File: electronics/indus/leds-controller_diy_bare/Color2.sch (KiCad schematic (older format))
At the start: 19 parts, among them Q2 Q_NPN_BCE, U1 TPS92513

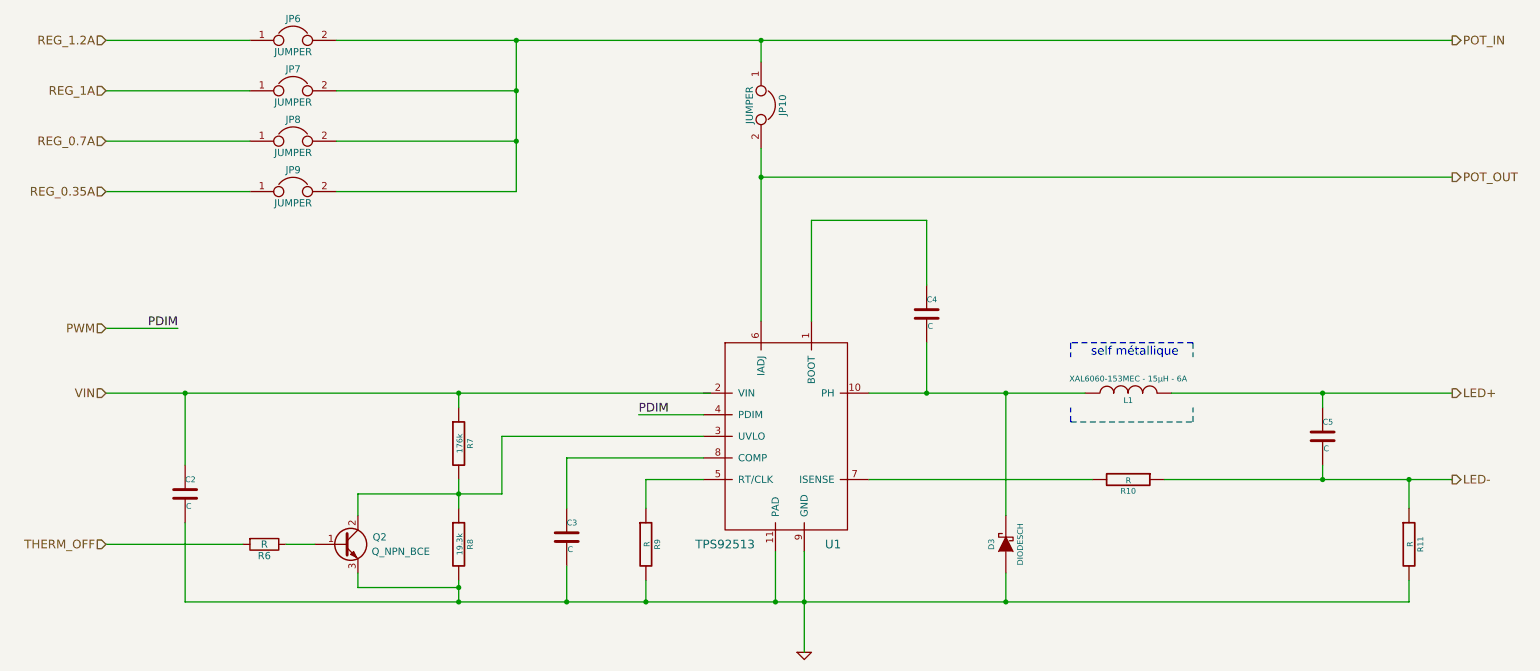
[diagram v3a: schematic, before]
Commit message: Added missing Capa & Resistor values
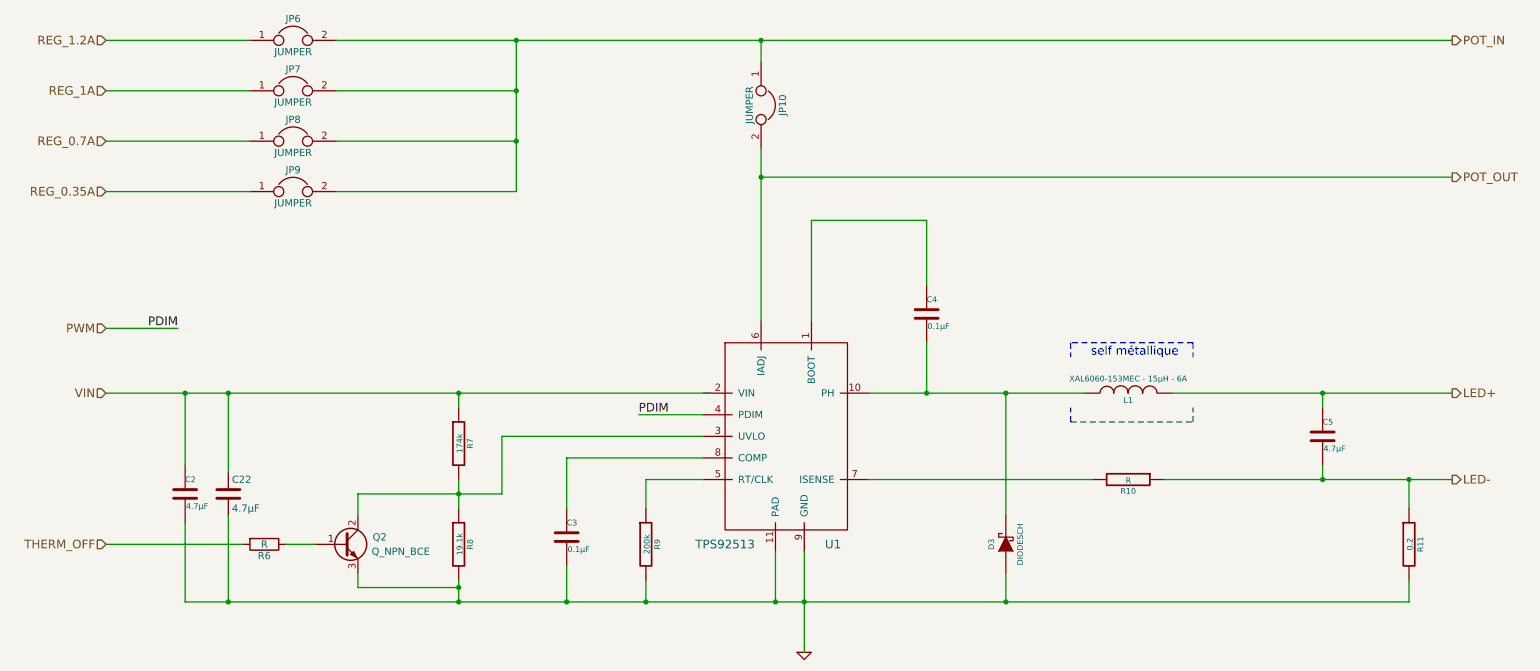
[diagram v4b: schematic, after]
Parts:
- added C22: 4.7µF, symbol C
- C2, C5: value C -> 4.7µF
- C3, C4: value C -> 0.1µF
- R11: value R -> 0.2
- R7: value 176k -> 174k
- R8: value 19.3k -> 19.1k
- R9: value R -> 200k
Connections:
- net GND: now also C22.2
- net VIN: now also C22.1
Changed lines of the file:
@@
 P 1750 4650
 F 0 "C2" H 1750 4750 40  0000 L CNN
-F 1 "C" H 1756 4565 40  0000 L CNN
+F 1 "4.7µF" H 1756 4565 40  0000 L CNN
 F 2 "" H 1788 4500 30  0000 C CNN
 F 3 "" H 1750 4650 60  0000 C CNN
@@
 P 3650 4300
 F 0 "R7" V 3730 4300 40  0000 C CNN
-F 1 "176k" V 3657 4301 40  0000 C CNN
+F 1 "174k" V 3657 4301 40  0000 C CNN
 F 2 "" V 3580 4300 30  0000 C CNN
 F 3 "" H 3650 4300 30  0000 C CNN
@@
 P 3650 5000
 F 0 "R8" V 3730 5000 40  0000 C CNN
-F 1 "19.3k" V 3657 5001 40  0000 C CNN
+F 1 "19.1k" V 3657 5001 40  0000 C CNN
 F 2 "" V 3580 5000 30  0000 C CNN
 F 3 "" H 3650 5000 30  0000 C CNN
@@
 P 4400 4950
 F 0 "C3" H 4400 5050 40  0000 L CNN
-F 1 "C" H 4406 4865 40  0000 L CNN
+F 1 "0.1µF" H 4406 4865 40  0000 L CNN
 F 2 "" H 4438 4800 30  0000 C CNN
 F 3 "" H 4400 4950 60  0000 C CNN
@@
 P 4950 5000
 F 0 "R9" V 5030 5000 40  0000 C CNN
-F 1 "R" V 4957 5001 40  0000 C CNN
+F 1 "200k" V 4957 5001 40  0000 C CNN
 F 2 "" V 4880 5000 30  0000 C CNN
 F 3 "" H 4950 5000 30  0000 C CNN
@@
 P 6900 3400
 F 0 "C4" H 6900 3500 40  0000 L CNN
-F 1 "C" H 6906 3315 40  0000 L CNN
+F 1 "0.1µF" H 6906 3315 40  0000 L CNN
 F 2 "" H 6938 3250 30  0000 C CNN
 F 3 "" H 6900 3400 60  0000 C CNN
@@
 P 9650 4250
 F 0 "C5" H 9650 4350 40  0000 L CNN
-F 1 "C" H 9656 4165 40  0000 L CNN
+F 1 "4.7µF" H 9656 4165 40  0000 L CNN
 F 2 "" H 9688 4100 30  0000 C CNN
 F 3 "" H 9650 4250 60  0000 C CNN
@@
 P 10250 5000
 F 0 "R11" V 10330 5000 40  0000 C CNN
-F 1 "R" V 10257 5001 40  0000 C CNN
+F 1 "0.2" V 10257 5001 40  0000 C CNN
 F 2 "" V 10180 5000 30  0000 C CNN
 F 3 "" H 10250 5000 30  0000 C CNN
@@
 POT_OUT
 Wire Wire Line
-	1200 3950 1750 3950
-Wire Wire Line
-	1750 3950 3650 3950
-Wire Wire Line
-	3650 3950 3650 3950
-Wire Wire Line
-	3650 3950 5400 3950
-Wire Wire Line
-	1750 5400 3650 5400
-Wire Wire Line
-	3650 5400 4400 5400
-Wire Wire Line
-	4400 5400 4950 5400
-Wire Wire Line
-	4950 5400 5850 5400
-Wire Wire Line
-	5850 5400 6050 5400
-Wire Wire Line
-	6050 5400 7450 5400
-Wire Wire Line
-	7450 5400 10250 5400
-Wire Wire Line
-	6050 5050 6050 5400
-Wire Wire Line
-	6050 5400 6050 5750
+	1200 3950 5400 3950
+Wire Wire Line
+	1750 5400 10250 5400
+Wire Wire Line
+	6050 5050 6050 5750
 Wire Wire Line
 	5850 5050 5850 5400
@@
 Connection ~ 6050 5400
 Wire Wire Line
-	3650 4550 3650 4650
-Wire Wire Line
-	3650 4650 3650 4750
+	3650 4550 3650 4750
 Wire Wire Line
 	3950 4650 3950 4250
@@
 	8750 3600 8750 3700
 Wire Wire Line
-	6500 3950 6900 3950
-Wire Wire Line
-	6900 3950 7450 3950
-Wire Wire Line
-	7450 3950 8000 3950
+	6500 3950 8000 3950
 Wire Wire Line
 	6100 3450 6100 2750
@@
 Connection ~ 6900 3950
 Wire Wire Line
-	8600 3950 9650 3950
-Wire Wire Line
-	9650 3950 10550 3950
+	8600 3950 10550 3950
 Wire Wire Line
 	9650 4050 9650 3950
@@
 	6500 4550 8050 4550
 Wire Wire Line
-	8550 4550 9650 4550
-Wire Wire Line
-	9650 4550 10250 4550
-Wire Wire Line
-	10250 4550 10550 4550
+	8550 4550 10550 4550
 Wire Wire Line
 	10250 4750 10250 4550
@@
 	1200 2550 2200 2550
 Wire Wire Line
-	2800 1500 4050 1500
-Wire Wire Line
-	4050 1500 5750 1500
-Wire Wire Line
-	5750 1500 10550 1500
+	2800 1500 10550 1500
 Wire Wire Line
 	2800 1850 4050 1850
 Wire Wire Line
-	4050 1500 4050 1850
-Wire Wire Line
-	4050 1850 4050 2200
-Wire Wire Line
-	4050 2200 4050 2550
+	4050 1500 4050 2550
 Connection ~ 4050 1500
 Wire Wire Line
@@
 Connection ~ 5750 2450
 Wire Wire Line
-	5750 2250 5750 2450
-Wire Wire Line
-	5750 2450 5750 3450
+	5750 2250 5750 3450
 Wire Wire Line
 	5750 1650 5750 1500
@@
 	1750 4850 1750 5400
 Wire Wire Line
-	3650 5250 3650 5300
-Wire Wire Line
-	3650 5300 3650 5400
+	3650 5250 3650 5400
 Wire Wire Line
 	3650 4050 3650 3950
@@
 	2950 4800 2950 4650
 Wire Wire Line
-	2950 4650 3650 4650
-Wire Wire Line
-	3650 4650 3950 4650
+	2950 4650 3950 4650
 Wire Wire Line
 	2950 5200 2950 5300
@@
 Wire Wire Line
 	2150 5000 1200 5000
+$Comp
+L C C22
+U 1 1 576AB4F9
+P 2050 4650
+F 0 "C22" H 2075 4750 50  0000 L CNN
+F 1 "4.7µF" H 2075 4550 50  0000 L CNN
+F 2 "" H 2088 4500 50  0000 C CNN
+F 3 "" H 2050 4650 50  0000 C CNN
+	1    2050 4650
+	1    0    0    -1
+$EndComp
+Wire Wire Line
+	2050 4500 2050 3950
+Connection ~ 2050 3950
+Wire Wire Line
+	2050 4800 2050 5400
+Connection ~ 2050 5400
 $EndSCHEMATC

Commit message: footprint with libraries
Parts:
- removed Q2: Q_NPN_BCE, symbol Q_NPN_BCE
- removed R6: R, symbol R
- C2, C22, C5: footprint (none) -> Capacitors_SMD:C_1206
- C3, C4: footprint (none) -> Capacitors_SMD:C_0805
- D3: footprint (none) -> Diodes_SMD:SOD-123
- R10: value R -> 1k; footprint (none) -> Resistors_SMD:R_0805
- R11: footprint (none) -> Resistors_SMD:R_1206
- R7, R8, R9: footprint (none) -> Resistors_SMD:R_0805
- U1: value TPS92513 -> TPS92513HVDGQT; footprint (none) -> risebox:BUCK_TPS92513_PowerPAD
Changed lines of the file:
@@
 P 5900 4050
 F 0 "U1" H 6250 3100 60  0000 C CNN
-F 1 "TPS92513" H 5500 3100 60  0000 C CNN
-F 2 "" H 6050 4150 60  0000 C CNN
+F 1 "TPS92513HVDGQT" H 5500 3100 60  0000 C CNN
+F 2 "risebox:BUCK_TPS92513_PowerPAD" H 6050 4150 60  0001 C CNN
 F 3 "" H 6050 4150 60  0000 C CNN
 	1    5900 4050
@@
 F 0 "C2" H 1750 4750 40  0000 L CNN
 F 1 "4.7µF" H 1756 4565 40  0000 L CNN
-F 2 "" H 1788 4500 30  0000 C CNN
+F 2 "Capacitors_SMD:C_1206" H 1788 4500 30  0001 C CNN
 F 3 "" H 1750 4650 60  0000 C CNN
 	1    1750 4650
@@
 $EndComp
 $Comp
-L GND-RESCUE-leds-controller #PWR11
+L GND-RESCUE-leds-controller #PWR012
 U 1 1 5766269A
 P 6050 5750
-F 0 "#PWR11" H 6050 5750 30  0001 C CNN
+F 0 "#PWR012" H 6050 5750 30  0001 C CNN
 F 1 "GND" H 6050 5680 30  0001 C CNN
 F 2 "" H 6050 5750 60  0000 C CNN
@@
 F 0 "R7" V 3730 4300 40  0000 C CNN
 F 1 "174k" V 3657 4301 40  0000 C CNN
-F 2 "" V 3580 4300 30  0000 C CNN
+F 2 "Resistors_SMD:R_0805" V 3580 4300 30  0001 C CNN
 F 3 "" H 3650 4300 30  0000 C CNN
 	1    3650 4300
@@
 F 0 "R8" V 3730 5000 40  0000 C CNN
 F 1 "19.1k" V 3657 5001 40  0000 C CNN
-F 2 "" V 3580 5000 30  0000 C CNN
+F 2 "Resistors_SMD:R_0805" V 3580 5000 30  0001 C CNN
 F 3 "" H 3650 5000 30  0000 C CNN
 	1    3650 5000
@@
 F 0 "C3" H 4400 5050 40  0000 L CNN
 F 1 "0.1µF" H 4406 4865 40  0000 L CNN
-F 2 "" H 4438 4800 30  0000 C CNN
+F 2 "Capacitors_SMD:C_0805" H 4438 4800 30  0001 C CNN
 F 3 "" H 4400 4950 60  0000 C CNN
 	1    4400 4950
@@
 F 0 "R9" V 5030 5000 40  0000 C CNN
 F 1 "200k" V 4957 5001 40  0000 C CNN
-F 2 "" V 4880 5000 30  0000 C CNN
+F 2 "Resistors_SMD:R_0805" V 4880 5000 30  0001 C CNN
 F 3 "" H 4950 5000 30  0000 C CNN
 	1    4950 5000
@@
 F 0 "C4" H 6900 3500 40  0000 L CNN
 F 1 "0.1µF" H 6906 3315 40  0000 L CNN
-F 2 "" H 6938 3250 30  0000 C CNN
+F 2 "Capacitors_SMD:C_0805" H 6938 3250 30  0001 C CNN
 F 3 "" H 6900 3400 60  0000 C CNN
 	1    6900 3400
@@
 F 0 "C5" H 9650 4350 40  0000 L CNN
 F 1 "4.7µF" H 9656 4165 40  0000 L CNN
-F 2 "" H 9688 4100 30  0000 C CNN
+F 2 "Capacitors_SMD:C_1206" H 9688 4100 30  0001 C CNN
 F 3 "" H 9650 4250 60  0000 C CNN
 	1    9650 4250
@@
 P 8300 4550
 F 0 "R10" V 8380 4550 40  0000 C CNN
-F 1 "R" V 8307 4551 40  0000 C CNN
-F 2 "" V 8230 4550 30  0000 C CNN
+F 1 "1k" V 8307 4551 40  0000 C CNN
+F 2 "Resistors_SMD:R_0805" V 8230 4550 30  0001 C CNN
 F 3 "" H 8300 4550 30  0000 C CNN
 	1    8300 4550
@@
 F 0 "R11" V 10330 5000 40  0000 C CNN
 F 1 "0.2" V 10257 5001 40  0000 C CNN
-F 2 "" V 10180 5000 30  0000 C CNN
+F 2 "Resistors_SMD:R_1206" V 10180 5000 30  0001 C CNN
 F 3 "" H 10250 5000 30  0000 C CNN
 	1    10250 5000
@@
 F 0 "D3" H 7450 5100 40  0000 C CNN
 F 1 "DIODESCH" H 7450 4900 40  0000 C CNN
-F 2 "" H 7450 5000 60  0000 C CNN
+F 2 "Diodes_SMD:SOD-123" H 7450 5000 60  0001 C CNN
 F 3 "" H 7450 5000 60  0000 C CNN
 	1    7450 5000
@@
 F 0 "JP6" H 2500 1650 50  0000 C CNN
 F 1 "JUMPER" H 2500 1420 50  0000 C CNN
-F 2 "" H 2500 1500 50  0000 C CNN
+F 2 "" H 2500 1500 50  0001 C CNN
 F 3 "" H 2500 1500 50  0000 C CNN
 	1    2500 1500
@@
 F 0 "JP7" H 2500 2000 50  0000 C CNN
 F 1 "JUMPER" H 2500 1770 50  0000 C CNN
-F 2 "" H 2500 1850 50  0000 C CNN
+F 2 "" H 2500 1850 50  0001 C CNN
 F 3 "" H 2500 1850 50  0000 C CNN
 	1    2500 1850
@@
 F 0 "JP8" H 2500 2350 50  0000 C CNN
 F 1 "JUMPER" H 2500 2120 50  0000 C CNN
-F 2 "" H 2500 2200 50  0000 C CNN
+F 2 "" H 2500 2200 50  0001 C CNN
 F 3 "" H 2500 2200 50  0000 C CNN
 	1    2500 2200
@@
 F 0 "JP9" H 2500 2700 50  0000 C CNN
 F 1 "JUMPER" H 2500 2470 50  0000 C CNN
-F 2 "" H 2500 2550 50  0000 C CNN
+F 2 "" H 2500 2550 50  0001 C CNN
 F 3 "" H 2500 2550 50  0000 C CNN
 	1    2500 2550
@@
 F 0 "JP10" H 5750 2100 50  0000 C CNN
 F 1 "JUMPER" H 5750 1870 50  0000 C CNN
-F 2 "" H 5750 1950 50  0000 C CNN
+F 2 "" H 5750 1950 50  0001 C CNN
 F 3 "" H 5750 1950 50  0000 C CNN
 	1    5750 1950
@@
 Connection ~ 3650 3950
 Connection ~ 3650 5400
-Wire Wire Line
-	2950 4800 2950 4650
-Wire Wire Line
-	2950 4650 3950 4650
-Wire Wire Line
-	2950 5200 2950 5300
-Wire Wire Line
-	2950 5300 3650 5300
-Connection ~ 3650 5300
-$Comp
-L Q_NPN_BCE Q2
-U 1 1 57662775
-P 2850 5000
-F 0 "Q2" H 3150 5050 50  0000 R CNN
-F 1 "Q_NPN_BCE" H 3450 4950 50  0000 R CNN
-F 2 "" H 3050 5100 50  0000 C CNN
-F 3 "" H 2850 5000 50  0000 C CNN
-	1    2850 5000
-	1    0    0    -1
-$EndComp
-Text HLabel 1200 5000 0    60   Input ~ 0
-THERM_OFF
-$Comp
-L R R6
-U 1 1 5766277D
-P 2300 5000
-F 0 "R6" V 2380 5000 50  0000 C CNN
-F 1 "R" V 2300 5000 50  0000 C CNN
-F 2 "" V 2230 5000 50  0000 C CNN
-F 3 "" H 2300 5000 50  0000 C CNN
-	1    2300 5000
-	0    1    1    0
-$EndComp
-Wire Wire Line
-	2450 5000 2650 5000
-Wire Wire Line
-	2150 5000 1200 5000
 $Comp
 L C C22
@@
 F 0 "C22" H 2075 4750 50  0000 L CNN
 F 1 "4.7µF" H 2075 4550 50  0000 L CNN
-F 2 "" H 2088 4500 50  0000 C CNN
+F 2 "Capacitors_SMD:C_1206" H 2088 4500 50  0001 C CNN
 F 3 "" H 2050 4650 50  0000 C CNN
 	1    2050 4650
@@
 	2050 4800 2050 5400
 Connection ~ 2050 5400
+Wire Wire Line
+	3650 4650 3950 4650
 $EndSCHEMATC

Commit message: fix some errors
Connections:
- net VIN: now also U1.2 (VIN)
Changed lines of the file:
@@
 Text HLabel 10550 4550 2    60   Output ~ 0
 LED-
-Text HLabel 1200 3950 0    60   Input ~ 0
+Text HLabel 1400 3950 0    60   Input ~ 0
 VIN
 $Comp
@@
 POT_OUT
 Wire Wire Line
-	1200 3950 5400 3950
+	1400 3950 5350 3950
 Wire Wire Line
 	1750 5400 10250 5400
@@
 	5750 1650 5750 1500
 Wire Wire Line
-	1750 4450 1750 3950
-Connection ~ 1750 3950
+	1750 4450 1950 3950
+Connection ~ 1950 3950
 Wire Wire Line
 	1750 4850 1750 5400

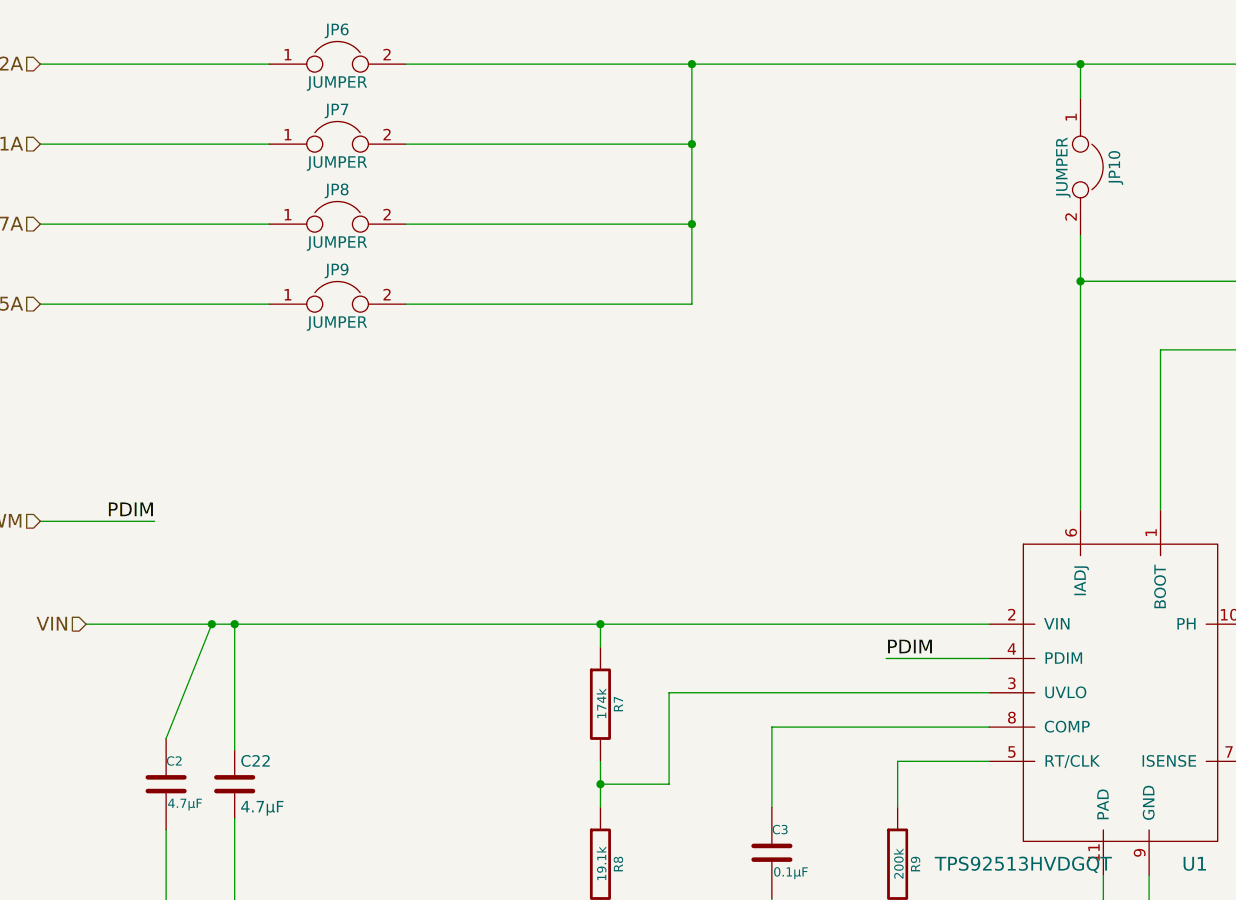
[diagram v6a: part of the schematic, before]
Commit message: add pinhead footprint
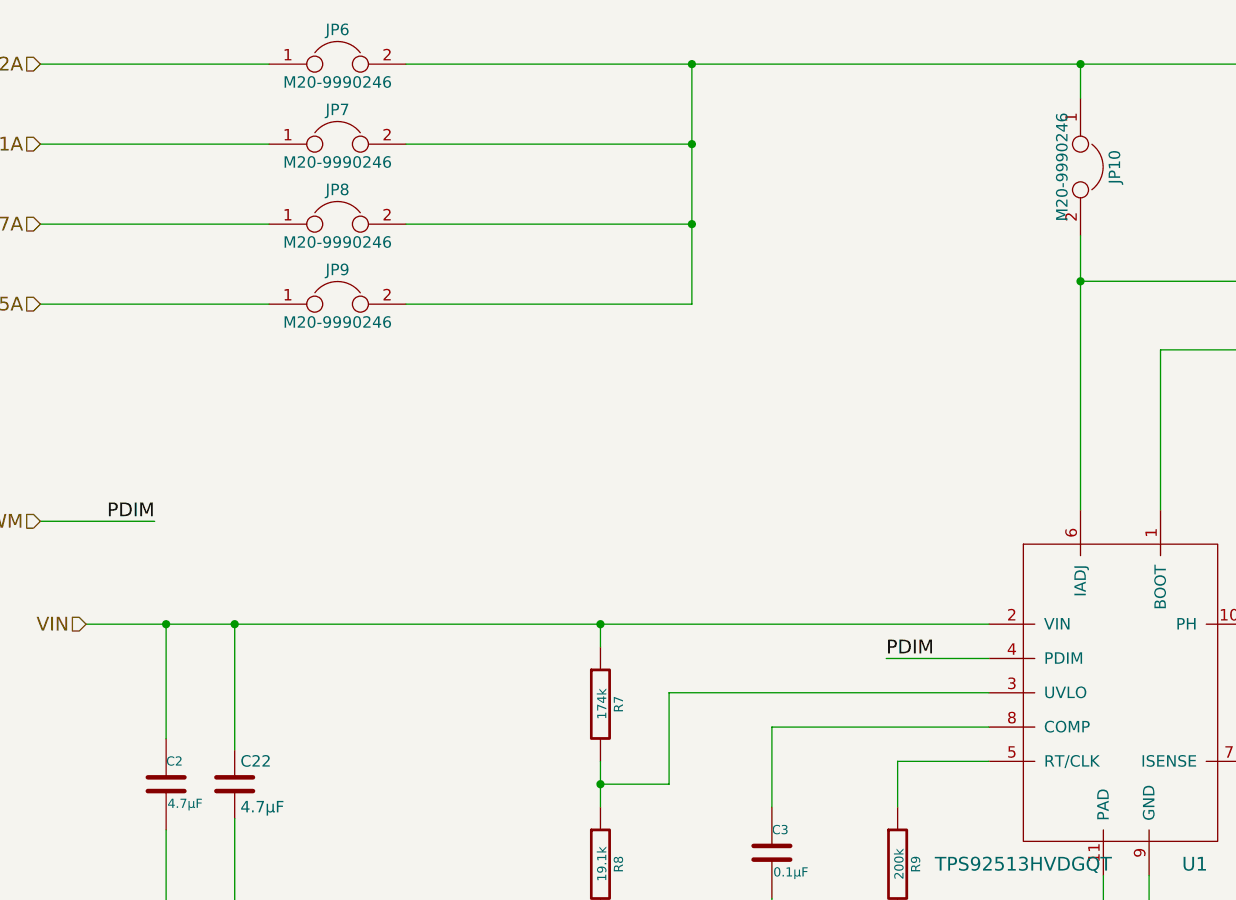
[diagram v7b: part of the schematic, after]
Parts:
- JP10, JP6, JP7, JP8, JP9: value JUMPER -> M20-9990246; footprint (none) -> Connect:PINHEAD1-2
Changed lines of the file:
@@
 P 2500 1500
 F 0 "JP6" H 2500 1650 50  0000 C CNN
-F 1 "JUMPER" H 2500 1420 50  0000 C CNN
-F 2 "" H 2500 1500 50  0001 C CNN
+F 1 "M20-9990246" H 2500 1420 50  0000 C CNN
+F 2 "Connect:PINHEAD1-2" H 2500 1500 50  0001 C CNN
 F 3 "" H 2500 1500 50  0000 C CNN
 	1    2500 1500
@@
 P 2500 1850
 F 0 "JP7" H 2500 2000 50  0000 C CNN
-F 1 "JUMPER" H 2500 1770 50  0000 C CNN
-F 2 "" H 2500 1850 50  0001 C CNN
+F 1 "M20-9990246" H 2500 1770 50  0000 C CNN
+F 2 "Connect:PINHEAD1-2" H 2500 1850 50  0001 C CNN
 F 3 "" H 2500 1850 50  0000 C CNN
 	1    2500 1850
@@
 P 2500 2200
 F 0 "JP8" H 2500 2350 50  0000 C CNN
-F 1 "JUMPER" H 2500 2120 50  0000 C CNN
-F 2 "" H 2500 2200 50  0001 C CNN
+F 1 "M20-9990246" H 2500 2120 50  0000 C CNN
+F 2 "Connect:PINHEAD1-2" H 2500 2200 50  0001 C CNN
 F 3 "" H 2500 2200 50  0000 C CNN
 	1    2500 2200
@@
 P 2500 2550
 F 0 "JP9" H 2500 2700 50  0000 C CNN
-F 1 "JUMPER" H 2500 2470 50  0000 C CNN
-F 2 "" H 2500 2550 50  0001 C CNN
+F 1 "M20-9990246" H 2500 2470 50  0000 C CNN
+F 2 "Connect:PINHEAD1-2" H 2500 2550 50  0001 C CNN
 F 3 "" H 2500 2550 50  0000 C CNN
 	1    2500 2550
@@
 P 5750 1950
 F 0 "JP10" H 5750 2100 50  0000 C CNN
-F 1 "JUMPER" H 5750 1870 50  0000 C CNN
-F 2 "" H 5750 1950 50  0001 C CNN
+F 1 "M20-9990246" H 5750 1870 50  0000 C CNN
+F 2 "Connect:PINHEAD1-2" H 5750 1950 50  0001 C CNN
 F 3 "" H 5750 1950 50  0000 C CNN
 	1    5750 1950
@@
 	5750 1650 5750 1500
 Wire Wire Line
-	1750 4450 1950 3950
-Connection ~ 1950 3950
+	1750 4450 1750 3950
+Connection ~ 1750 3950
 Wire Wire Line
 	1750 4850 1750 5400
